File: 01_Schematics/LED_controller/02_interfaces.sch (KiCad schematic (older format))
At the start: 20 parts, among them J10 TB-02, J11 TB-02, J12 TB-03, J13 TB-02, J8 TB-02, J9 TB-03

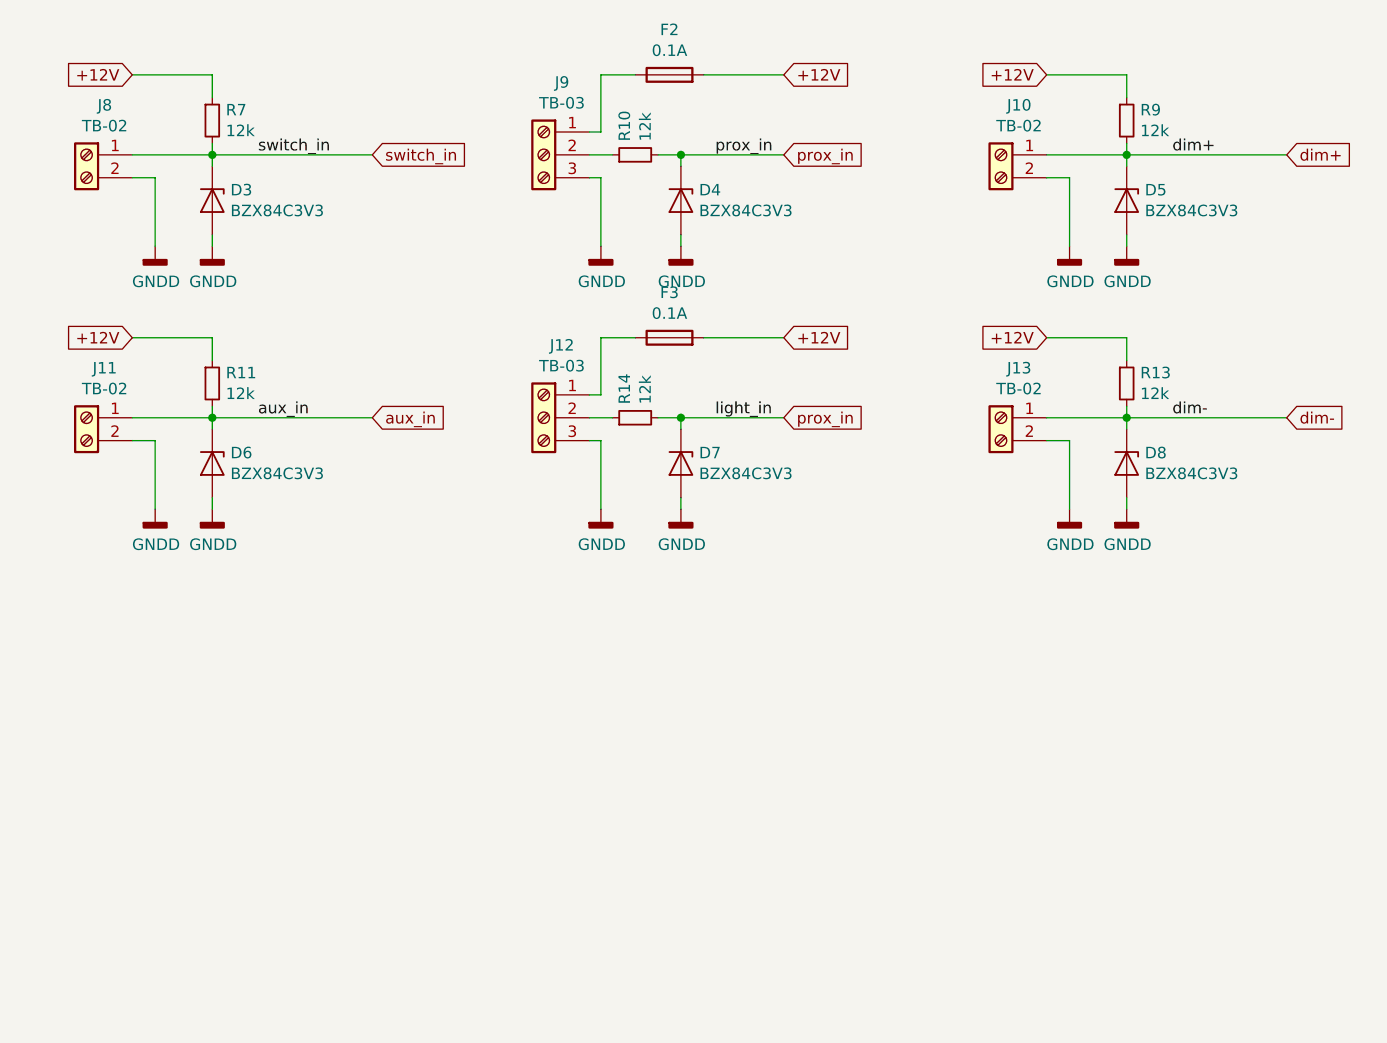
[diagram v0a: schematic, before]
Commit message: - Добавлена печатная плата; - Добавлены файлы посадочных мест использованных компонентов и STEP модели; - Добавлены файлы механической сборки (Solidworks);
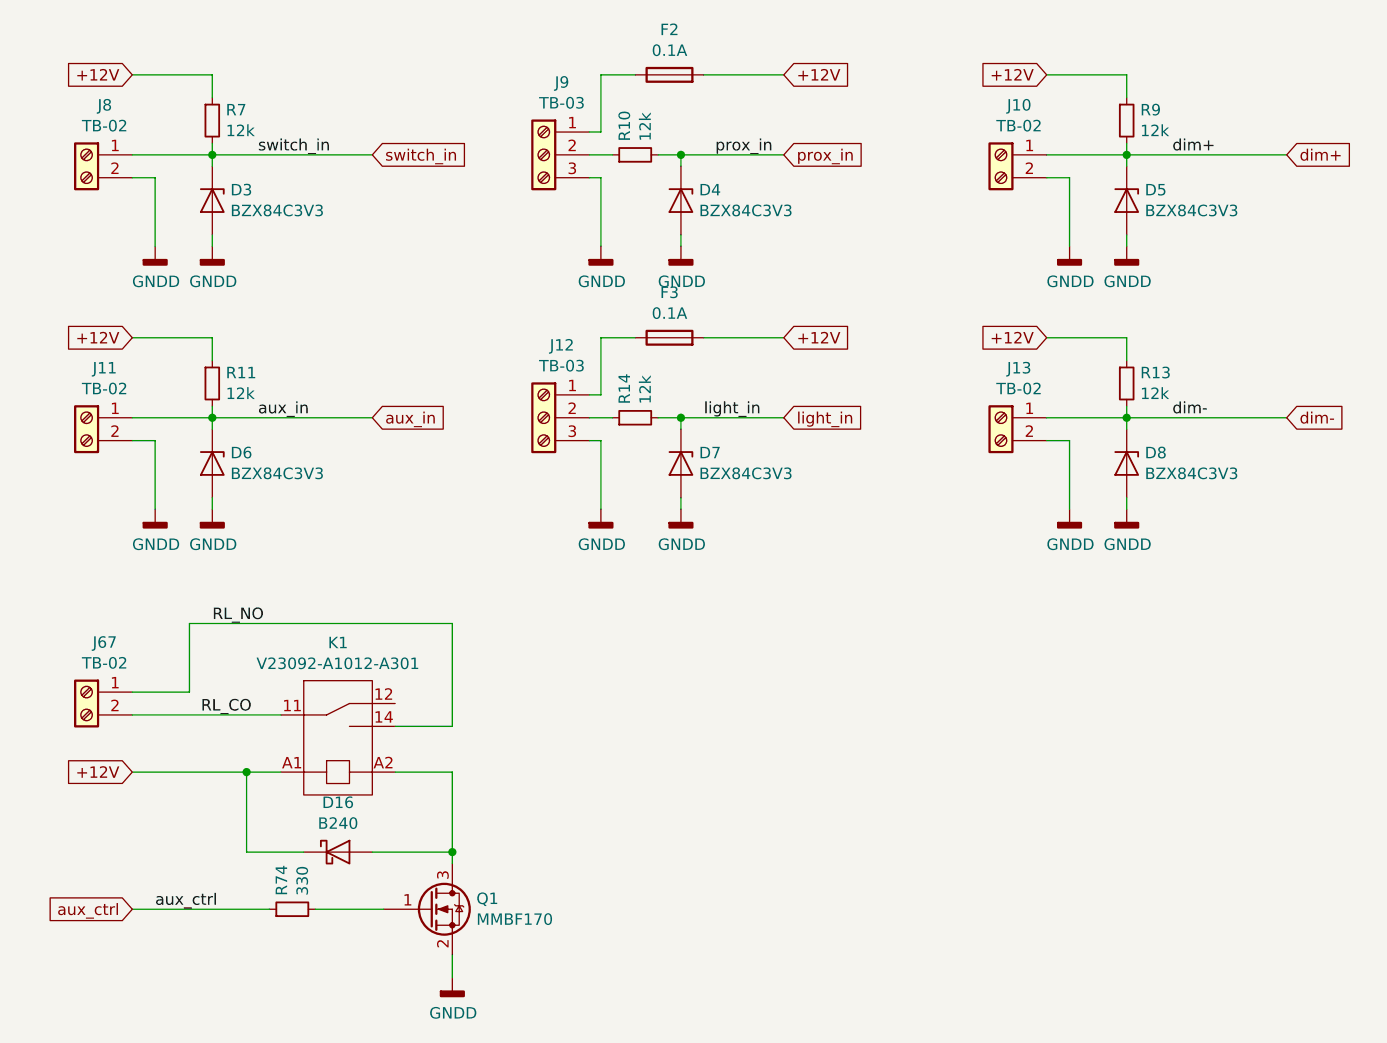
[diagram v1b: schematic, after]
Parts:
- added D16: B240, Diode_SMD:D_SMB, symbol Diode:B240
- added J67: TB-02, extras:TB-02_metric, symbol Connector:Screw_Terminal_01x02
- added K1: V23092-A1012-A301, extras:Relay_TE_V23092, symbol extras:V23092-A1012-A301
- added Q1: MMBF170, Package_TO_SOT_SMD:SOT-23, symbol Transistor_FET:MMBF170
- added R74: 330, Resistor_SMD:R_0805_2012Metric_Pad1.15x1.40mm_HandSolder, symbol Device:R_Small
- J10, J11, J13, J8: footprint TerminalBlock:TerminalBlock_bornier-2_P5.08mm -> extras:TB-02_metric; partnum TB-02 -> 300-021-12
- J12, J9: footprint TerminalBlock:TerminalBlock_bornier-3_P5.08mm -> extras:TB-03_metric; partnum TB-03 -> 300-031-12
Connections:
- net +12V: now also D16.1 (K), K1.A1
- net GNDD: now also Q1.2 (S)
- net prox_in: no longer D7.1 (K), R14.2
- new net: D16.2 (A), K1.A2, Q1.3 (D)
- new net: Q1.1 (G), R74.2
- new net RL_CO: J67.2 (Pin_2), K1.11
- new net RL_NO: J67.1 (Pin_1), K1.14
- new net aux_ctrl: R74.1
- new net light_in: D7.1 (K), R14.2
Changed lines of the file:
@@
 F 0 "J8" H 2620 2067 50  0000 C CNN
 F 1 "TB-02" H 2620 1976 50  0000 C CNN
-F 2 "TerminalBlock:TerminalBlock_bornier-2_P5.08mm" H 2700 1850 50  0001 C CNN
+F 2 "extras:TB-02_metric" H 2700 1850 50  0001 C CNN
 F 3 "~" H 2700 1850 50  0001 C CNN
-F 4 "TB-02" H 2700 1850 50  0001 C CNN "partnum"
+F 4 "300-021-12" H 2700 1850 50  0001 C CNN "partnum"
 	1    2700 1850
 	-1   0    0    -1
@@
 F 0 "J11" H 2620 3217 50  0000 C CNN
 F 1 "TB-02" H 2620 3126 50  0000 C CNN
-F 2 "TerminalBlock:TerminalBlock_bornier-2_P5.08mm" H 2700 3000 50  0001 C CNN
+F 2 "extras:TB-02_metric" H 2700 3000 50  0001 C CNN
 F 3 "~" H 2700 3000 50  0001 C CNN
-F 4 "TB-02" H 2700 3000 50  0001 C CNN "partnum"
+F 4 "300-021-12" H 2700 3000 50  0001 C CNN "partnum"
 	1    2700 3000
 	-1   0    0    -1
@@
 F 0 "J9" H 4620 2167 50  0000 C CNN
 F 1 "TB-03" H 4620 2076 50  0000 C CNN
-F 2 "TerminalBlock:TerminalBlock_bornier-3_P5.08mm" H 4700 1850 50  0001 C CNN
+F 2 "extras:TB-03_metric" H 4700 1850 50  0001 C CNN
 F 3 "~" H 4700 1850 50  0001 C CNN
-F 4 "TB-03" H 4700 1850 50  0001 C CNN "partnum"
+F 4 "300-031-12" H 4700 1850 50  0001 C CNN "partnum"
 	1    4700 1850
 	-1   0    0    -1
@@
 F 0 "J10" H 6620 2067 50  0000 C CNN
 F 1 "TB-02" H 6620 1976 50  0000 C CNN
-F 2 "TerminalBlock:TerminalBlock_bornier-2_P5.08mm" H 6700 1850 50  0001 C CNN
+F 2 "extras:TB-02_metric" H 6700 1850 50  0001 C CNN
 F 3 "~" H 6700 1850 50  0001 C CNN
-F 4 "TB-02" H 6700 1850 50  0001 C CNN "partnum"
+F 4 "300-021-12" H 6700 1850 50  0001 C CNN "partnum"
 	1    6700 1850
 	-1   0    0    -1
@@
 F 0 "J13" H 6620 3217 50  0000 C CNN
 F 1 "TB-02" H 6620 3126 50  0000 C CNN
-F 2 "TerminalBlock:TerminalBlock_bornier-2_P5.08mm" H 6700 3000 50  0001 C CNN
+F 2 "extras:TB-02_metric" H 6700 3000 50  0001 C CNN
 F 3 "~" H 6700 3000 50  0001 C CNN
-F 4 "TB-02" H 6700 3000 50  0001 C CNN "partnum"
+F 4 "300-021-12" H 6700 3000 50  0001 C CNN "partnum"
 	1    6700 3000
 	-1   0    0    -1
@@
 	1    0    0    -1
 $EndComp
-Text Label 5450 3000 0    50   ~ 0
+Text Label 5400 3000 0    50   ~ 0
 light_in
 Connection ~ 5300 3000
@@
 F 0 "J12" H 4620 3317 50  0000 C CNN
 F 1 "TB-03" H 4620 3226 50  0000 C CNN
-F 2 "TerminalBlock:TerminalBlock_bornier-3_P5.08mm" H 4700 3000 50  0001 C CNN
+F 2 "extras:TB-03_metric" H 4700 3000 50  0001 C CNN
 F 3 "~" H 4700 3000 50  0001 C CNN
-F 4 "TB-03" H 4700 3000 50  0001 C CNN "partnum"
+F 4 "300-031-12" H 4700 3000 50  0001 C CNN "partnum"
 	1    4700 3000
 	-1   0    0    -1
 $EndComp
 Text GLabel 5750 3000 2    50   Input ~ 0
-prox_in
+light_in
 Wire Wire Line
 	5750 3000 5300 3000
@@
 	0    -1   -1   0
 $EndComp
+$Comp
+L Connector:Screw_Terminal_01x02 J67
+U 1 1 5C9A78A8
+P 2700 4200
+F 0 "J67" H 2620 4417 50  0000 C CNN
+F 1 "TB-02" H 2620 4326 50  0000 C CNN
+F 2 "extras:TB-02_metric" H 2700 4200 50  0001 C CNN
+F 3 "~" H 2700 4200 50  0001 C CNN
+F 4 "300-021-12" H 2700 4200 50  0001 C CNN "partnum"
+	1    2700 4200
+	-1   0    0    -1
+$EndComp
+$Comp
+L extras:V23092-A1012-A301 K1
+U 1 1 5C9AB6C0
+P 3650 4150
+F 0 "K1" H 3800 4315 50  0000 C CNN
+F 1 "V23092-A1012-A301" H 3800 4224 50  0000 C CNN
+F 2 "extras:Relay_TE_V23092" H 3850 4200 50  0001 C CNN
+F 3 "" H 3850 4200 50  0001 C CNN
+	1    3650 4150
+	1    0    0    -1
+$EndComp
+Wire Wire Line
+	2900 4300 3550 4300
+Wire Wire Line
+	4050 4350 4300 4350
+Wire Wire Line
+	4300 4350 4300 3900
+Wire Wire Line
+	4300 3900 3150 3900
+Wire Wire Line
+	3150 3900 3150 4200
+Wire Wire Line
+	3150 4200 2900 4200
+Text Label 3200 4300 0    50   ~ 0
+RL_CO
+Text Label 3250 3900 0    50   ~ 0
+RL_NO
+Text GLabel 2900 4550 0    50   Input ~ 0
++12V
+Wire Wire Line
+	2900 4550 3400 4550
+$Comp
+L Transistor_FET:MMBF170 Q1
+U 1 1 5C9B738A
+P 4200 5150
+F 0 "Q1" H 4405 5196 50  0000 L CNN
+F 1 "MMBF170" H 4405 5105 50  0000 L CNN
+F 2 "Package_TO_SOT_SMD:SOT-23" H 4400 5075 50  0001 L CIN
+F 3 "https://www.diodes.com/assets/Datasheets/ds30104.pdf" H 4200 5150 50  0001 L CNN
+	1    4200 5150
+	1    0    0    -1
+$EndComp
+$Comp
+L power:GNDD #PWR032
+U 1 1 5C9B748A
+P 4300 5450
+F 0 "#PWR032" H 4300 5200 50  0001 C CNN
+F 1 "GNDD" H 4304 5295 50  0000 C CNN
+F 2 "" H 4300 5450 50  0001 C CNN
+F 3 "" H 4300 5450 50  0001 C CNN
+	1    4300 5450
+	1    0    0    -1
+$EndComp
+Wire Wire Line
+	4300 5350 4300 5450
+Wire Wire Line
+	4050 4550 4300 4550
+$Comp
+L Device:R_Small R?
+U 1 1 5C9C4164
+P 3600 5150
+AR Path="/5BC4A73F/5C9C4164" Ref="R?"  Part="1"
+AR Path="/5C0A4430/5C9C4164" Ref="R?"  Part="1"
+AR Path="/5BC5F278/5C9C4164" Ref="R74"  Part="1"
+F 0 "R74" H 3659 5196 50  0000 L CNN
+F 1 "330" H 3659 5105 50  0000 L CNN
+F 2 "Resistor_SMD:R_0805_2012Metric_Pad1.15x1.40mm_HandSolder" H 3600 5150 50  0001 C CNN
+F 3 "~" H 3600 5150 50  0001 C CNN
+F 4 "RC0805FR-07330RL" H 3600 5150 50  0001 C CNN "partnum"
+	1    3600 5150
+	0    -1   -1   0
+$EndComp
+Wire Wire Line
+	3700 5150 4000 5150
+Text GLabel 2900 5150 0    50   Input ~ 0
+aux_ctrl
+Wire Wire Line
+	2900 5150 3500 5150
+Text Label 3000 5150 0    50   ~ 0
+aux_ctrl
+$Comp
+L Diode:B240 D16
+U 1 1 5C9CEDC0
+P 3800 4900
+F 0 "D16" H 3800 5116 50  0000 C CNN
+F 1 "B240" H 3800 5025 50  0000 C CNN
+F 2 "Diode_SMD:D_SMB" H 3800 4725 50  0001 C CNN
+F 3 "http://www.jameco.com/Jameco/Products/ProdDS/1538777.pdf" H 3800 4900 50  0001 C CNN
+	1    3800 4900
+	1    0    0    -1
+$EndComp
+Wire Wire Line
+	3650 4900 3400 4900
+Wire Wire Line
+	3400 4900 3400 4550
+Connection ~ 3400 4550
+Wire Wire Line
+	3400 4550 3550 4550
+Wire Wire Line
+	3950 4900 4300 4900
+Wire Wire Line
+	4300 4550 4300 4900
+Connection ~ 4300 4900
+Wire Wire Line
+	4300 4900 4300 4950
 $EndSCHEMATC
